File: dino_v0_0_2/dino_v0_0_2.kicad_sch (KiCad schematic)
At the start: 16 parts, among them SW2 RESET_BTN, U20 74LS163, U27 74LS74, U56 74HC14, U6 74LS163, U7 74LS138, U8 74LS138, Y1 4MHz

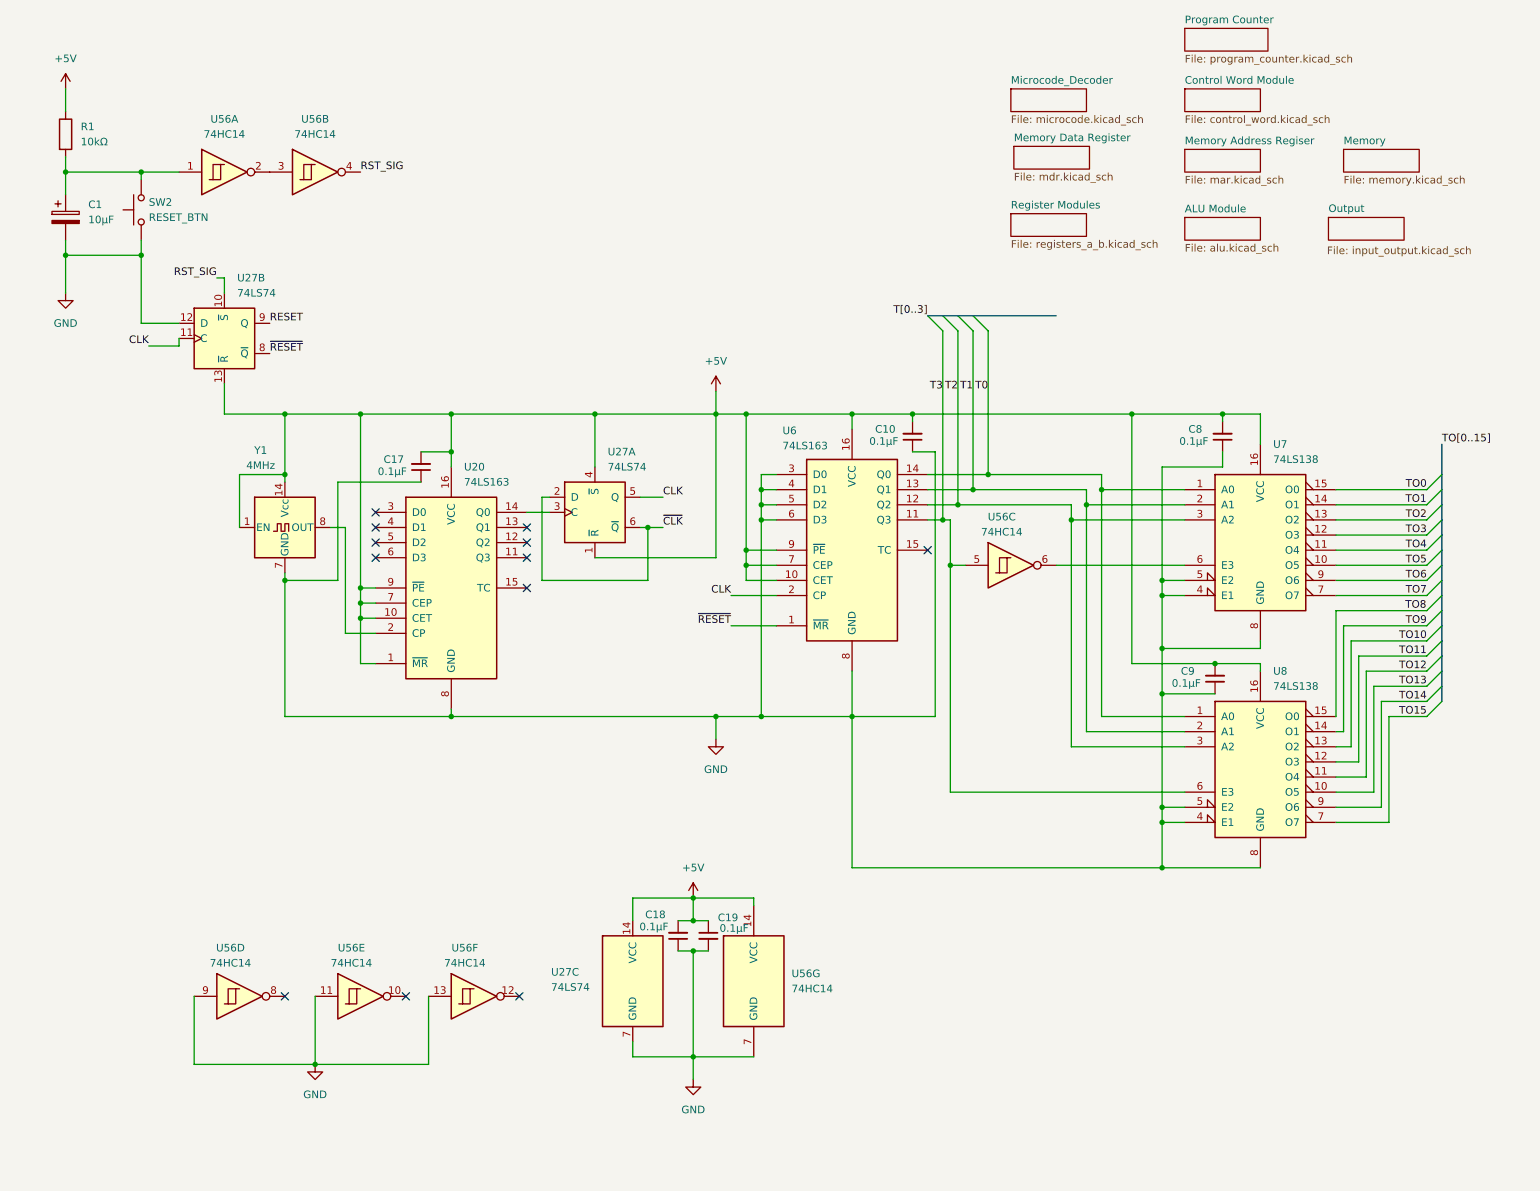
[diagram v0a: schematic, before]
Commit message: feat(dino): complete v0.0.3 schematic — all 11 sheets netlist-clean
- wire MAR sheet: '373 LO/HI latches, 2x '245 M-bus drive, A15 decode
  (ROM_EN/~RAM_EN), LE stamps off /MAR_LO_LOAD//MAR_HI_LOAD
- fix PC_MAR_MUX polarity: PC '245s enabled on bit14=0, inverted vs
  bit-map convention (PC=1); add ~PC_MAR_MUX inverter, relabel U13/U14
- wire all 7 control-word bus taps [15:9] (SA0-2, END, PC_UP,
  PC_MAR_MUX, HALT) — label pairs had no wire between them
- untie NONE/NC '138 outputs: totem-pole bus fight on every microword;
  each unused output now individually no_connect
- build END (U61 NOR: ~MR = RESET|END, sync T-state clear) and HALT
  (T-state freeze via CET, clock keeps running)
- build COND/JNZ (U62: ~PC_LOAD = taken-JNZ | unconditional-JMP)
- claim src code 111 as /SW_OUT: IN port — DIP switches through 10k
  pull-ups onto W bus via '244; LED bank active-high off OB0-7
- add U66 missing power unit + decouplers (C63-C66)
- tools: kicad_gen_sheet.py (declarative YAML/JSON sheet generator,
  deterministic uuid5, collision-checked), kicad_xsheet_audit.py
  (cross-sheet contract audit); archive stale testing-strategy doc
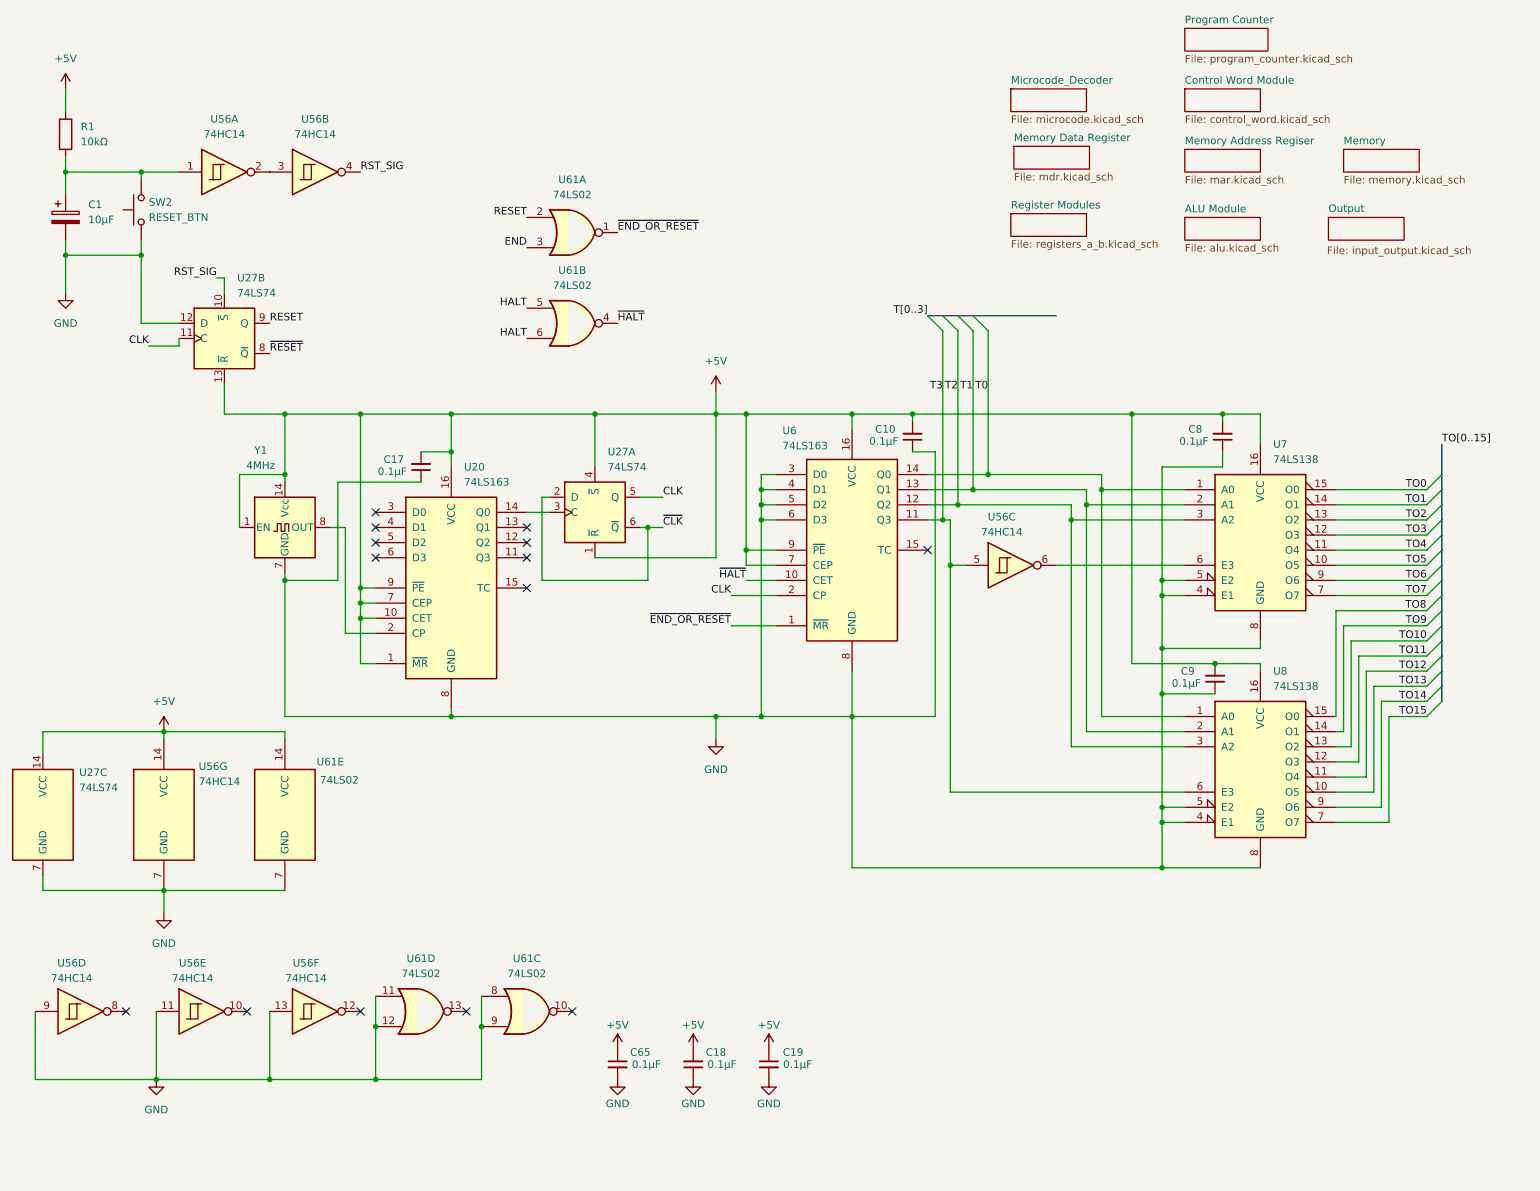
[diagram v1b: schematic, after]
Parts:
- added C65: 0.1µF, symbol Device:C_Small
- added U61: 74LS02, symbol 74xx:74LS02
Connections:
- net +5V: now also C65.1, U61.14 (VCC); no longer U6.10 (CET)
- net GND: now also C65.2, U61.11, U61.12, U61.7 (GND), U61.8, U61.9
- net RESET: now also U61.2
- net ~{RESET}: no longer U6.1 (~{MR})
- new net END: U61.3
- new net HALT: U61.5, U61.6
- new net ~{END_OR_RESET}: U6.1 (~{MR}), U61.1
- new net ~{HALT}: U6.10 (CET), U61.4
- no-connect marks 12 -> 14
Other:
- moved on the sheet: C18, C19, U27C, U56D, U56E, U56F, U56G

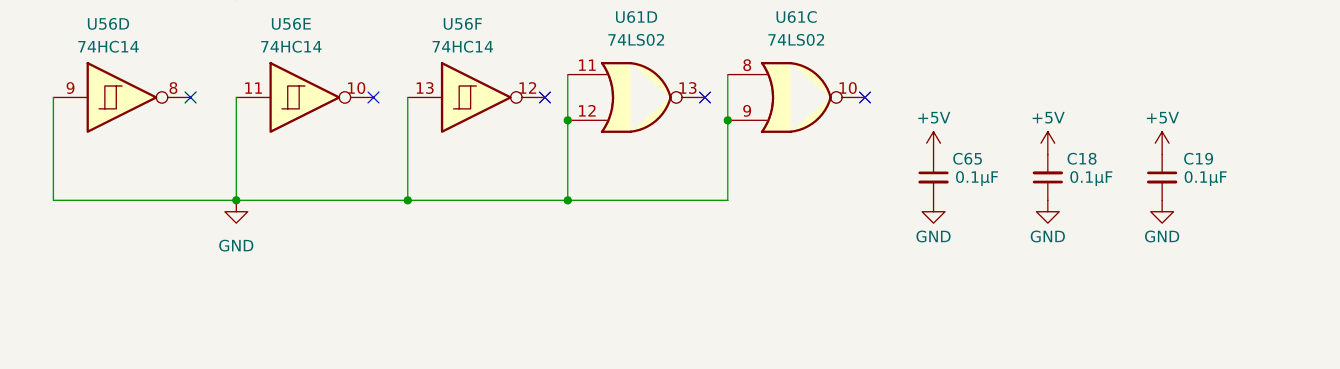
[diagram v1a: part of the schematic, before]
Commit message: feat(dino): generate + stamp per-sheet I/O contracts
Each module's boundary signals (IN/OUT/BIDIR with counterpart sheets)
derived from the kicad-cli netlist and placed as a text block on the
physical sheet, so a bench rig knows exactly what to drive and observe
per board. kicad_contracts.py regenerates both the markdown and the
stamps idempotently; stamping verified electrically neutral.
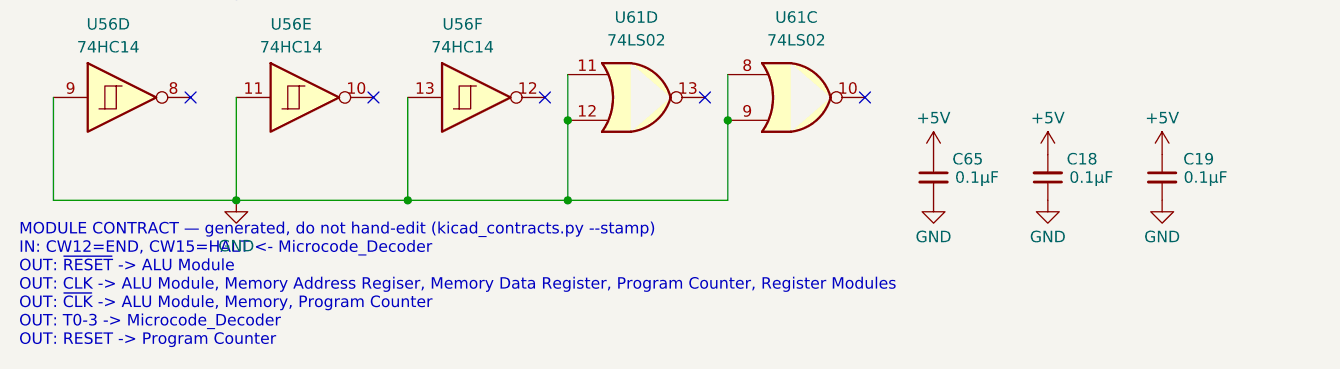
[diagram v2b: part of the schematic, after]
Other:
- note added: "MODULE CONTRACT — generated, do not hand-edit (kicad_contracts.py --stamp) IN: CW12=END, CW15=HALT <- Microcode_Decoder OUT: ~{RESET} -> ALU Module OUT: CLK -> ALU Module, Memory Address Regiser, Memory Data Register, Program Counter, Register Modules OUT: ~{CLK} -> ALU Module, Memory, Program Counter OUT: T0-3 -> Microcode_Decoder OUT: RESET -> Program Counter"
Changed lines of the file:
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@@
 	)
 	(embedded_fonts no)
+	(text "MODULE CONTRACT — generated, do not hand-edit (kicad_contracts.py --stamp)\nIN: CW12=END, CW15=HALT <- Microcode_Decoder\nOUT: ~{RESET} -> ALU Module\nOUT: CLK -> ALU Module, Memory Address Regiser, Memory Data Register, Program Counter, Register Modules\nOUT: ~{CLK} -> ALU Module, Memory, Program Counter\nOUT: T0-3 -> Microcode_Decoder\nOUT: RESET -> Program Counter"
+		(exclude_from_sim no)
+		(at 15.24 211.93 0)
+		(effects
+			(font
+				(size 1.27 1.27)
+			)
+			(justify left bottom)
+		)
+	)
 )
